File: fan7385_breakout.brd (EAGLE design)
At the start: 28.6 x 14 mm, 13 parts

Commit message: autorouted
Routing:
- net D2/VS2: track 0.00 -> 46.4 mm, vias 0 -> 1
- net HO2/G2: track 0.00 -> 42.1 mm, vias 0 -> 1
- net VDD: track 0.00 -> 32.0 mm, vias 0 -> 1
- net D1/VS1: track 0.00 -> 29.5 mm, vias 0 -> 2
- net HO1/G1: track 0.00 -> 27.3 mm, vias 0 -> 1
- net S2: track 0.00 -> 20.2 mm, vias 0 -> 1
- net VB1: track 0.00 -> 11.0 mm
- net VB2: track 0.00 -> 7.38 mm
- net S1: track 0.00 -> 7.05 mm
- net IN2: track 0.00 -> 2.03 mm
- net IN1: track 0.00 -> 2.03 mm

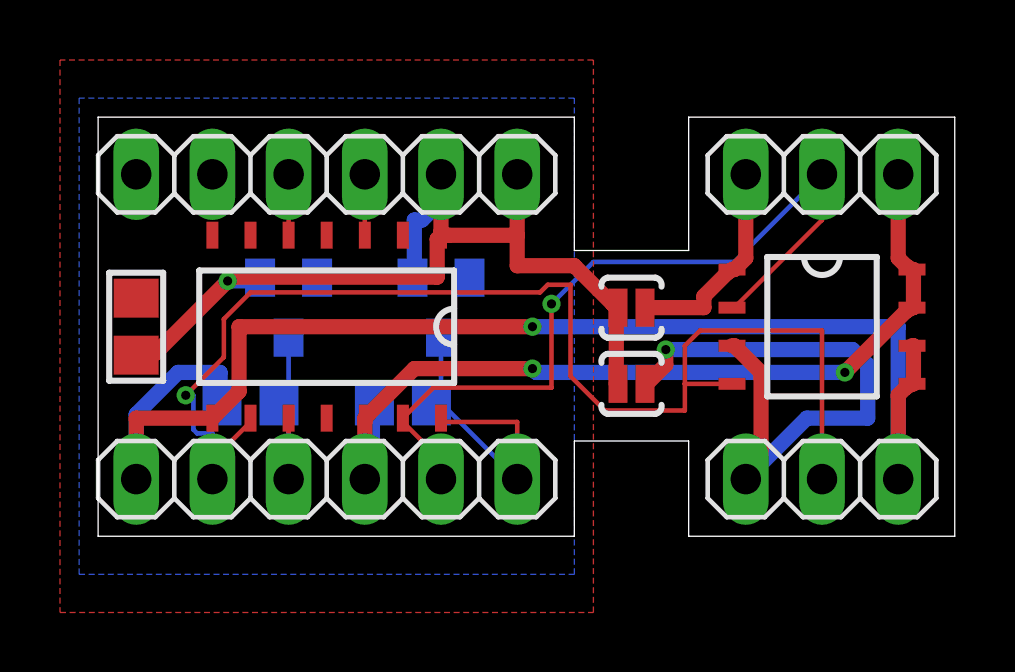
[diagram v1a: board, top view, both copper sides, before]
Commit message: polygons on the mosfer high-current signals
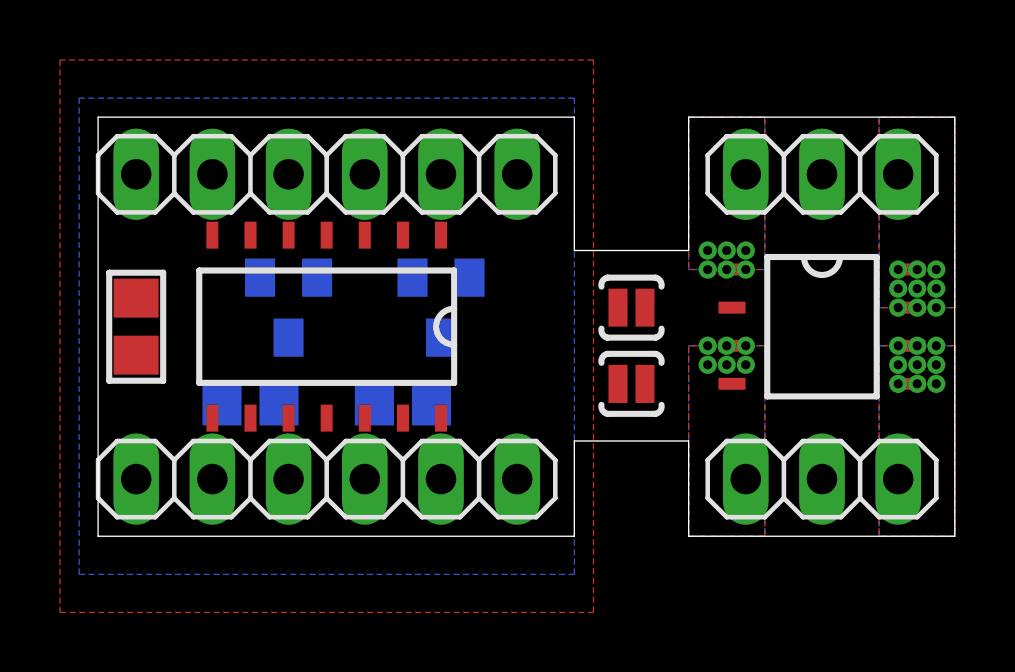
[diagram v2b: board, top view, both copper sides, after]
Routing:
- net D2/VS2: track 46.4 -> 0.00 mm, vias 1 -> 9
- net HO2/G2: track 42.1 -> 0.00 mm, vias 1 -> 0
- net VDD: track 32.0 -> 0.00 mm, vias 1 -> 0
- net D1/VS1: track 29.5 -> 0.00 mm, vias 2 -> 9
- net HO1/G1: track 27.3 -> 0.00 mm, vias 1 -> 0
- net S2: track 20.2 -> 0.00 mm, vias 1 -> 6
- net VB1: track 11.0 -> 0.00 mm
- net VB2: track 7.38 -> 0.00 mm
- net S1: track 7.05 -> 0.00 mm, vias 0 -> 6
- net IN2: track 2.03 -> 0.00 mm
- net IN1: track 2.03 -> 0.00 mm
- added copper zone on layer 1, net D1/VS1
- added copper zone on layer 16, net D1/VS1
- added copper zone on layer 1, net D2/VS2
- added copper zone on layer 16, net D2/VS2
- added copper zone on layer 1, net S1
- added copper zone on layer 16, net S1
- added copper zone on layer 1, net S2
- added copper zone on layer 16, net S2

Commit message: make the signal back from drains to the driver normal instead of high-power
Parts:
- added SJ3, SJ4: SOLDERJUMPERTRACE, SparkFun-Passives:SJ_2S-TRACE
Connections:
- removed net D1/VS1: CBOOT1.1, FET.7, FET.8, GATEDRV.12, JP2.4, JP4.3
- removed net D2/VS2: CBOOT2.1, FET.5, FET.6, GATEDRV.8, JP2.1, JP3.3
- new net D1: CBOOT1.1, FET.7, FET.8, JP2.4, JP4.3, SJ3.2
- new net D2: CBOOT2.1, FET.5, FET.6, JP2.1, JP3.3, SJ4.2
- new net VS1: GATEDRV.12, SJ3.1
- new net VS2: GATEDRV.8, SJ4.1
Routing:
- added copper zone on layer 1, net D1
- added copper zone on layer 16, net D1
- added copper zone on layer 1, net D2
- added copper zone on layer 16, net D2
- removed copper zone on layer 1, net D1/VS1
- removed copper zone on layer 16, net D1/VS1
- removed copper zone on layer 1, net D2/VS2
- removed copper zone on layer 16, net D2/VS2
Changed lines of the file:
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@@
 <attribute name="VALUE" x="20.32" y="8.89" size="1.27" layer="27"/>
+</element>
+<element name="SJ3" library="SparkFun-Passives" package="SJ_2S-TRACE" value="SOLDERJUMPERTRACE" x="25.4" y="8.89" smashed="yes" rot="MR180">
+<attribute name="NAME" x="24.4475" y="7.62" size="0.4064" layer="26" rot="MR180"/>
+</element>
+<element name="SJ4" library="SparkFun-Passives" package="SJ_2S-TRACE" value="SOLDERJUMPERTRACE" x="25.4" y="5.08" smashed="yes" rot="MR180">
+<attribute name="NAME" x="24.4475" y="3.81" size="0.4064" layer="26" rot="MR180"/>
 </element>
 </elements>
@@
 <wire x1="6.35" y1="1.905" x2="6.35" y2="3.935" width="0" layer="19" extent="1-1"/>
 </signal>
-<signal name="D2/VS2" class="2">
+<signal name="D2" class="2">
 <contactref element="FET" pad="6"/>
 <contactref element="FET" pad="5"/>
-<contactref element="GATEDRV" pad="8"/>
 <contactref element="CBOOT2" pad="1"/>
 <contactref element="JP2" pad="1"/>
@@
 <via x="27.94" y="6.35" extent="1-16" drill="0.3048" shape="square"/>
 <via x="26.67" y="6.35" extent="1-16" drill="0.3048" shape="square"/>
-<wire x1="4.13" y1="4.445" x2="3.81" y2="3.935" width="0" layer="19" extent="1-16"/>
-<wire x1="1.27" y1="1.905" x2="3.81" y2="3.935" width="0" layer="19" extent="1-1"/>
-<wire x1="26.67" y1="5.08" x2="4.13" y2="4.445" width="0" layer="19" extent="16-16"/>
-</signal>
-<signal name="D1/VS1" class="2">
+<contactref element="SJ4" pad="2"/>
+<wire x1="26.67" y1="5.08" x2="25.908" y2="5.08" width="0" layer="19" extent="16-16"/>
+<wire x1="4.13" y1="4.445" x2="25.908" y2="5.08" width="0" layer="19" extent="16-16"/>
+<wire x1="1.27" y1="1.905" x2="4.13" y2="4.445" width="0" layer="19" extent="16-16"/>
+</signal>
+<signal name="D1" class="2">
 <contactref element="FET" pad="8"/>
 <contactref element="FET" pad="7"/>
-<contactref element="GATEDRV" pad="12"/>
 <contactref element="CBOOT1" pad="1"/>
 <contactref element="JP2" pad="4"/>
@@
 <via x="27.305" y="8.89" extent="1-16" drill="0.3048" shape="square"/>
 <via x="27.94" y="8.89" extent="1-16" drill="0.3048" shape="square"/>
-<wire x1="9.21" y1="4.445" x2="8.89" y2="3.935" width="0" layer="19" extent="1-16"/>
-<wire x1="8.89" y1="1.905" x2="8.89" y2="3.935" width="0" layer="19" extent="1-1"/>
-<wire x1="26.67" y1="7.62" x2="9.21" y2="4.445" width="0" layer="19" extent="16-16"/>
+<contactref element="SJ3" pad="2"/>
+<wire x1="26.67" y1="8.89" x2="25.908" y2="8.89" width="0" layer="19" extent="16-16"/>
+<wire x1="9.21" y1="4.445" x2="25.908" y2="8.89" width="0" layer="19" extent="16-16"/>
+<wire x1="8.89" y1="1.905" x2="9.21" y2="4.445" width="0" layer="19" extent="16-16"/>
+</signal>
+<signal name="VS1">
+<contactref element="GATEDRV" pad="12"/>
+<contactref element="SJ3" pad="1"/>
+<wire x1="8.89" y1="3.935" x2="24.892" y2="8.89" width="0" layer="19" extent="1-16"/>
+</signal>
+<signal name="VS2">
+<contactref element="GATEDRV" pad="8"/>
+<contactref element="SJ4" pad="1"/>
+<wire x1="3.81" y1="3.935" x2="24.892" y2="5.08" width="0" layer="19" extent="1-16"/>
 </signal>
 </signals>

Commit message: one more signal rename
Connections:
- net D1: no longer JP2.4
- net D2: no longer JP2.1
- net VS1: now also JP2.4
- net VS2: now also JP2.1
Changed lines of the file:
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@@
 <contactref element="FET" pad="5"/>
 <contactref element="CBOOT2" pad="1"/>
-<contactref element="JP2" pad="1"/>
 <contactref element="JP3" pad="3"/>
 <polygon width="0.4064" layer="1" isolate="0.254" thermals="no">
@@
 <wire x1="26.67" y1="5.08" x2="25.908" y2="5.08" width="0" layer="19" extent="16-16"/>
 <wire x1="4.13" y1="4.445" x2="25.908" y2="5.08" width="0" layer="19" extent="16-16"/>
-<wire x1="1.27" y1="1.905" x2="4.13" y2="4.445" width="0" layer="19" extent="16-16"/>
 </signal>
 <signal name="D1" class="2">
@@
 <contactref element="FET" pad="7"/>
 <contactref element="CBOOT1" pad="1"/>
-<contactref element="JP2" pad="4"/>
 <contactref element="JP4" pad="3"/>
 <polygon width="0.4064" layer="1" isolate="0.254" thermals="no">
@@
 <wire x1="26.67" y1="8.89" x2="25.908" y2="8.89" width="0" layer="19" extent="16-16"/>
 <wire x1="9.21" y1="4.445" x2="25.908" y2="8.89" width="0" layer="19" extent="16-16"/>
-<wire x1="8.89" y1="1.905" x2="9.21" y2="4.445" width="0" layer="19" extent="16-16"/>
 </signal>
 <signal name="VS1">
 <contactref element="GATEDRV" pad="12"/>
 <contactref element="SJ3" pad="1"/>
+<contactref element="JP2" pad="4"/>
 <wire x1="8.89" y1="3.935" x2="24.892" y2="8.89" width="0" layer="19" extent="1-16"/>
+<wire x1="8.89" y1="1.905" x2="8.89" y2="3.935" width="0" layer="19" extent="1-1"/>
 </signal>
 <signal name="VS2">
 <contactref element="GATEDRV" pad="8"/>
 <contactref element="SJ4" pad="1"/>
+<contactref element="JP2" pad="1"/>
 <wire x1="3.81" y1="3.935" x2="24.892" y2="5.08" width="0" layer="19" extent="1-16"/>
+<wire x1="1.27" y1="1.905" x2="3.81" y2="3.935" width="0" layer="19" extent="1-1"/>
 </signal>
 </signals>

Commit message: one more signal rename
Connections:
- net D1: no longer CBOOT1.1
- net D2: no longer CBOOT2.1
- net VS1: now also CBOOT1.1
- net VS2: now also CBOOT2.1
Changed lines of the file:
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@@
 <contactref element="FET" pad="6"/>
 <contactref element="FET" pad="5"/>
-<contactref element="CBOOT2" pad="1"/>
 <contactref element="JP3" pad="3"/>
 <polygon width="0.4064" layer="1" isolate="0.254" thermals="no">
@@
 <contactref element="SJ4" pad="2"/>
 <wire x1="26.67" y1="5.08" x2="25.908" y2="5.08" width="0" layer="19" extent="16-16"/>
-<wire x1="4.13" y1="4.445" x2="25.908" y2="5.08" width="0" layer="19" extent="16-16"/>
 </signal>
 <signal name="D1" class="2">
 <contactref element="FET" pad="8"/>
 <contactref element="FET" pad="7"/>
-<contactref element="CBOOT1" pad="1"/>
 <contactref element="JP4" pad="3"/>
 <polygon width="0.4064" layer="1" isolate="0.254" thermals="no">
@@
 <contactref element="SJ3" pad="2"/>
 <wire x1="26.67" y1="8.89" x2="25.908" y2="8.89" width="0" layer="19" extent="16-16"/>
-<wire x1="9.21" y1="4.445" x2="25.908" y2="8.89" width="0" layer="19" extent="16-16"/>
 </signal>
 <signal name="VS1">
@@
 <contactref element="SJ3" pad="1"/>
 <contactref element="JP2" pad="4"/>
-<wire x1="8.89" y1="3.935" x2="24.892" y2="8.89" width="0" layer="19" extent="1-16"/>
+<contactref element="CBOOT1" pad="1"/>
+<wire x1="9.21" y1="4.445" x2="24.892" y2="8.89" width="0" layer="19" extent="16-16"/>
+<wire x1="8.89" y1="3.935" x2="9.21" y2="4.445" width="0" layer="19" extent="1-16"/>
 <wire x1="8.89" y1="1.905" x2="8.89" y2="3.935" width="0" layer="19" extent="1-1"/>
 </signal>
@@
 <contactref element="SJ4" pad="1"/>
 <contactref element="JP2" pad="1"/>
-<wire x1="3.81" y1="3.935" x2="24.892" y2="5.08" width="0" layer="19" extent="1-16"/>
+<contactref element="CBOOT2" pad="1"/>
+<wire x1="4.13" y1="4.445" x2="24.892" y2="5.08" width="0" layer="19" extent="16-16"/>
+<wire x1="3.81" y1="3.935" x2="4.13" y2="4.445" width="0" layer="19" extent="1-16"/>
 <wire x1="1.27" y1="1.905" x2="3.81" y2="3.935" width="0" layer="19" extent="1-1"/>
 </signal>

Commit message: minor layout adjustments
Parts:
- moved SJ1 2.69 mm to (15.9, 6.99)
- moved SJ2 2.29 mm to (15.9, 8.89)
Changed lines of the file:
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@@
 <attribute name="VALUE" x="13.335" y="8.255" size="0.4064" layer="28" ratio="10" rot="MR180"/>
 </element>
-<element name="SJ1" library="SparkFun-Passives" package="SJ_2S-NO" value="SOLDERJUMPERNO" x="17.78" y="5.08" smashed="yes"/>
-<element name="SJ2" library="SparkFun-Passives" package="SJ_2S-NO" value="SOLDERJUMPERNO" x="17.78" y="7.62" smashed="yes"/>
+<element name="SJ1" library="SparkFun-Passives" package="SJ_2S-NO" value="SOLDERJUMPERNO" x="15.875" y="6.985" smashed="yes"/>
+<element name="SJ2" library="SparkFun-Passives" package="SJ_2S-NO" value="SOLDERJUMPERNO" x="15.875" y="8.89" smashed="yes"/>
 <element name="JP1" library="pinhead" package="1X06" value="" x="7.62" y="12.065" smashed="yes">
 <attribute name="VALUE" x="0" y="8.89" size="1.27" layer="27"/>
@@
 <attribute name="VALUE" x="20.32" y="8.89" size="1.27" layer="27"/>
 </element>
-<element name="SJ3" library="SparkFun-Passives" package="SJ_2S-TRACE" value="SOLDERJUMPERTRACE" x="25.4" y="8.89" smashed="yes" rot="MR180">
-<attribute name="NAME" x="24.4475" y="7.62" size="0.4064" layer="26" rot="MR180"/>
-</element>
-<element name="SJ4" library="SparkFun-Passives" package="SJ_2S-TRACE" value="SOLDERJUMPERTRACE" x="25.4" y="5.08" smashed="yes" rot="MR180">
-<attribute name="NAME" x="24.4475" y="3.81" size="0.4064" layer="26" rot="MR180"/>
-</element>
+<element name="SJ3" library="SparkFun-Passives" package="SJ_2S-TRACE" value="SOLDERJUMPERTRACE" x="25.4" y="8.89" smashed="yes" rot="MR180"/>
+<element name="SJ4" library="SparkFun-Passives" package="SJ_2S-TRACE" value="SOLDERJUMPERTRACE" x="25.4" y="5.08" smashed="yes" rot="MR180"/>
 </elements>
 <signals>
@@
 <contactref element="JP1" pad="6"/>
 <contactref element="JP1" pad="5"/>
-<wire x1="17.33" y1="5.08" x2="17.33" y2="7.62" width="0" layer="19" extent="1-1"/>
-<wire x1="13.97" y1="12.065" x2="17.33" y2="7.62" width="0" layer="19" extent="1-1"/>
+<wire x1="15.425" y1="6.985" x2="15.425" y2="8.89" width="0" layer="19" extent="1-1"/>
+<wire x1="13.97" y1="12.065" x2="15.425" y2="8.89" width="0" layer="19" extent="1-1"/>
 <wire x1="11.43" y1="12.065" x2="13.97" y2="12.065" width="0" layer="19" extent="1-1"/>
 <wire x1="11.43" y1="10.035" x2="11.43" y2="12.065" width="0" layer="19" extent="1-1"/>
@@
 <via x="20.955" y="9.525" extent="1-16" drill="0.3048" shape="square"/>
 <via x="21.59" y="9.525" extent="1-16" drill="0.3048" shape="square"/>
-<wire x1="20.32" y1="8.89" x2="18.23" y2="7.62" width="0" layer="19" extent="1-1"/>
+<wire x1="20.32" y1="8.89" x2="16.325" y2="8.89" width="0" layer="19" extent="1-1"/>
 </signal>
 <signal name="S2" class="2">
@@
 <via x="20.955" y="5.715" extent="1-16" drill="0.3048" shape="square"/>
 <via x="20.32" y="5.715" extent="1-16" drill="0.3048" shape="square"/>
-<wire x1="20.32" y1="5.715" x2="18.23" y2="5.08" width="0" layer="19" extent="1-1"/>
+<wire x1="20.32" y1="5.715" x2="16.325" y2="6.985" width="0" layer="19" extent="1-1"/>
 </signal>
 <signal name="IN1">
